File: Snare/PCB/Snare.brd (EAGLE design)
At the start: 100 x 50 mm, 93 parts, among them IC1 LM741P, IC10 LM741P, IC6 LM741P, IC7 LM741P, IC8 LM741P, IC9 LM741P, Q3 2N2222A, Q4 2N2222A, T1 2N3904, T5 2N3904, T6 2N3904

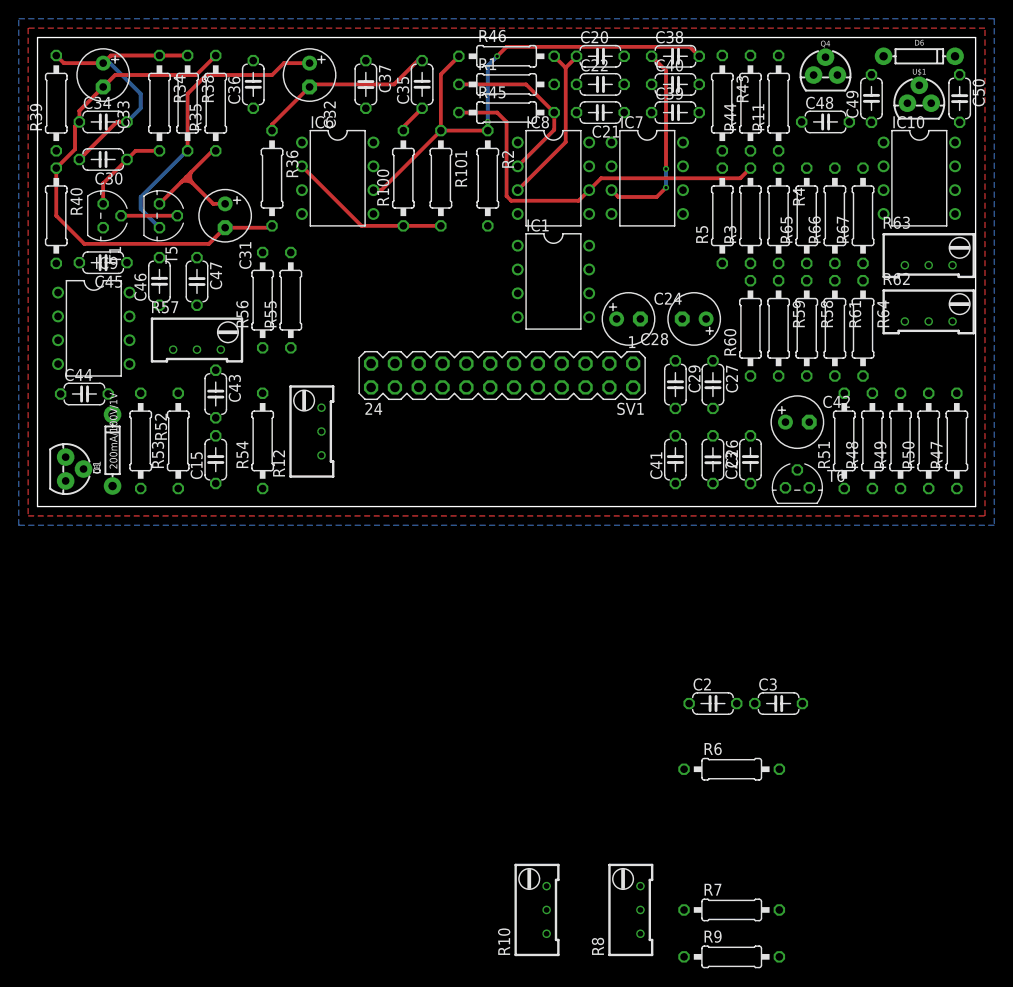
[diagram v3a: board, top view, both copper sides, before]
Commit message: Finished PCB
Finished the snare PCB
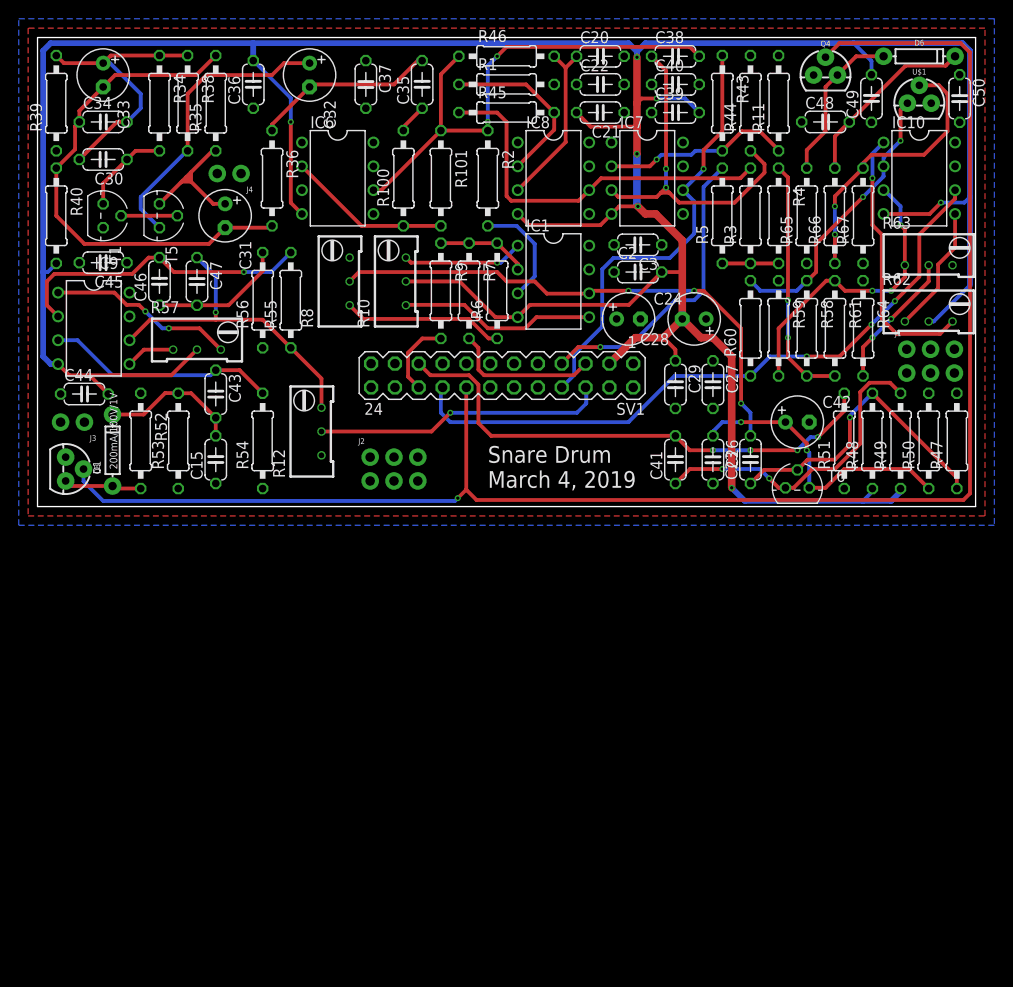
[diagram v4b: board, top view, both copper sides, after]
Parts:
- added J1, J2: (no value), SparkFun-Connectors:2X3-NS
- added J3, J4: (no value), SparkFun-Connectors:1X02_NO_SILK
- moved R9 77.5 mm to (43.0, 23.0), turned to 270 degrees
- moved R8 73.8 mm to (32.0, 24.0)
- moved R7 71.7 mm to (46.0, 23.0), turned to 270 degrees
- moved R10 68.7 mm to (38.0, 24.0)
- moved R6 56.8 mm to (49.0, 23.0), turned to 90 degrees
- moved C3 51.1 mm to (64.0, 27.9), turned to 180 degrees
- moved C2 46.7 mm to (64.0, 25.0)
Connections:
- removed net N$44: C46.1, C47.2
- new net N$8: C46.1, C47.2, R56.2
- net DRUM_OUTPUT: no longer R56.2
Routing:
- net -12V: track 0.00 -> 368.8 mm, vias 0 -> 7
- net TRIGGER: track 0.00 -> 172.3 mm, vias 0 -> 1
- net SW1: track 0.00 -> 71.4 mm, vias 0 -> 3
- net CC_INPUT: track 0.00 -> 56.8 mm, vias 0 -> 3
- net OUTPUT: track 0.00 -> 55.2 mm, vias 0 -> 4
- net POT2A: track 0.00 -> 47.0 mm, vias 0 -> 1
- net DRUM_OUTPUT: track 0.00 -> 34.5 mm, vias 0 -> 1
- net N$38: track 0.00 -> 33.8 mm, vias 0 -> 2
- net N$43: track 0.00 -> 32.8 mm, vias 0 -> 1
- net N$37: track 0.00 -> 32.7 mm, vias 0 -> 1
- net POT2B: track 0.00 -> 32.2 mm, vias 0 -> 1
- net N$48: track 0.00 -> 32.0 mm, vias 0 -> 3
- net POT1A: track 0.00 -> 31.2 mm, vias 0 -> 1
- net N$39: track 0.00 -> 31.1 mm, vias 0 -> 2
- net N$49: track 0.00 -> 30.4 mm, vias 0 -> 2
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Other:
- board text added: "Snare Drum March 4, 2019"

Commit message: Finished Silkscreen
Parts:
- removed C38: 1nF, resistor:C050-024X044
- removed C41: 2.2u, resistor:C050-024X044
- removed C42: 10uF, rcl:E2,5-6
- removed C43, C44, C45, C49, C50: 0.1uF, resistor:C050-024X044
- removed C47: 33nF, resistor:C050-024X044
- removed D6: 200mA/100V/1V, SparkFun-DiscreteSemi:DIODE-1N4148
- removed R100, R51: 47k, resistor:0207/10
- removed R101: 100k, resistor:0207/10
- removed R34: 680k, resistor:0207/10
- removed R39, R40: 2k, resistor:0207/10
- removed R46: 15k, resistor:0207/10
- removed R49: 10k, resistor:0207/10
- removed R50: 220, resistor:0207/10
- added C10, C6, C9: 0.1uF, resistor:C050-024X044
- added C13, C14, C16: 10uF, rcl:E2,5-6
- added C17, C18: 1u, resistor:C050-024X044
- added C4: 1nF, resistor:C050-024X044
- added D2: 200mA/100V/1V, SparkFun-DiscreteSemi:DIODE-1N4148
- added R13: 1k, resistor:0207/10
- added R14, R16: 100k, resistor:0207/10
- added R15, R17, R18: 10k, resistor:0207/10
- added TRIM3, TRIM4, TRIM6: 10k, rcl:RTRIM64W
- C15: value 0.33uF -> 10uF; device resistor:C050-024X044 -> rcl:E2,5-6
- C2: value 0.1uF -> 1nF
- C20: value 1nF -> 0.33uF
- C23: value 2.2u -> 0.1uF
- C24, C28: value 10uF -> 0.1uF; device rcl:E2,5-6 -> resistor:C050-024X044
- C26, C29: value 1u -> 0.1uF
- C27: value 1u -> 33nF
- C3: value 0.1uF -> 10uF; device resistor:C050-024X044 -> rcl:E2,5-6
- C30: value 0.1uF -> 2.2u
- C31: value 10uF -> 1u; device rcl:E2,5-6 -> resistor:C050-024X044
- C32: value 10uF -> 2.2u; device rcl:E2,5-6 -> resistor:C050-024X044
- R1: value 2k -> 15k
- R10: device rcl:RTRIM64W -> resistor:0207/10
- R11: value 4.7k -> 2k
- R12: value 10k -> 4.7k; device rcl:RTRIM64W -> resistor:0207/10
- R2: value 100k -> 47k
- R3, R4: value 10k -> 2k
- R35: value 1k -> 10k
- R36: value 100k -> 10k
- R38: value 4.7k -> 1k
- R43: value 2k -> 220
- R44: value 15k -> 10k
- R45: value 10k -> 47k
- R5: value 10k -> 15k
- R6: value 1k -> 2k
- R7: value 10k -> 4.7k
- R8: value 10k -> 680k; device rcl:RTRIM64W -> resistor:0207/10
- R9: value 10k -> 100k
- moved D1 95.7 mm to (94.0, 48.0), turned to 0 degrees
- moved Q3 91.2 mm to (84.0, 46.0), turned to 0 degrees
- moved Q4 91.2 mm to (3.00, 4.00), turned to 270 degrees
- moved C33 82.7 mm to (81.0, 9.00), turned to 0 degrees
- moved R4 77.0 mm to (2.00, 31.0)
- moved C30 76.1 mm to (76.0, 5.00), turned to 90 degrees
- moved R3 75.0 mm to (2.00, 43.0)
- moved C23 72.1 mm to (7.00, 26.0), turned to 180 degrees
- moved C26 67.4 mm to (5.00, 12.0), turned to 0 degrees
- moved C3 59.8 mm to (7.00, 46.0), turned to 270 degrees
- moved C20 59.4 mm to (19.0, 5.00), turned to 90 degrees
- moved C31 58.1 mm to (72.0, 5.00)
- moved C32 56.6 mm to (68.0, 5.00), turned to 90 degrees
- moved C27 56.1 mm to (17.0, 24.0)
- moved C22 52.6 mm to (19.0, 12.0), turned to 270 degrees
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- renumbered C34 to C5, C35 to C1, C36 to C8, C37 to C7, C39 to C12, C40 to C11, C46 to C25, C48 to C19, IC10 to IC4, IC7 to IC3, IC8 to IC2, IC9 to IC5, R47 to R41, R48 to R42, R52 to R20, R53 to R27, R54 to R29, R55 to R31, R56 to R32, R57 to TRIM5, R58 to R21, R59 to R28, R60 to R30, R61 to R22, R62 to TRIM2, R63 to TRIM1, R64 to R23, R65 to R19, R66 to R25, R67 to R26, T1 to Q1, T5 to Q2, T6 to Q6, U$1 to Q5
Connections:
- net +12V: now also C15.+, C17.2, C21.2, C23.1, C28.2, C9.2, R3.1, R43.2; no longer C22.2, C24.+, C27.2, C3.2, C45.1, C50.2, R39.1, R50.2
- net -12V: now also C10.2, C16.-, C18.1, C24.2, C26.2, C29.2, R4.2, R44.1, TRIM4.2; no longer C2.2, C21.2, C28.-, C29.1, C44.2, C49.2, R10.2, R40.2, R49.1
- net AGND: now also C10.1, C15.-, C16.+, C17.1, C18.2, C20.1, C23.2, C24.1, C26.1, C28.1, C29.1, C31.2, C33.-, C4.2, C9.1, R14.2, R45.1, R5.2, R6.2, R7.2, TRIM6.1; no longer C15.1, C2.1, C20.2, C22.1, C24.-, C26.2, C27.1, C28.+, C29.2, C3.1, C42.-, C44.1, C45.2, C49.1, C50.1, R1.2, R11.2, R12.1, R2.2, R44.2, R51.1
- net CC_INPUT: now also C30.2, IC6.6, TRIM3.2; no longer C23.2, IC1.6, R8.2
- net DRUM_OUTPUT: now also C27.1, TRIM6.3; no longer C47.1, R12.3
- net LOW_FREQ_WN: now also R10.1, R15.2; no longer R3.2, R45.1
- net N$1: now also R15.1, R17.1, R18.2; no longer R3.1, R4.2, R5.1
- net N$2: now also IC6.2, R35.1, R36.1, R38.2; no longer IC1.2, R6.2, R7.1, R9.1
- net N$20: now also C6.1, R8.2; no longer C30.1, R34.2
- net N$21: now also C14.-, C3.-, R13.2, R16.2, R4.1; no longer C31.-, C33.-, R35.2, R36.2, R40.1
- net N$23: now also IC1.2, R2.1, R9.2; no longer IC6.2, R100.1, R101.2
- net N$27: now also R11.2, R7.1; no longer R11.1, R43.2
- net N$28: now also R2.2; no longer R100.2
- net N$3: now also R38.1, TRIM3.1; no longer R6.1, R8.1
- net N$30: now also C13.+, R12.2; no longer C32.+, R38.2
- net N$32: now also C2.1, R5.1; no longer C38.1, R44.1
- net N$33: now also R10.2, R6.1; no longer R1.1, R45.2
- net N$34: now also C4.1, R1.2; no longer C20.1, R46.2
- net N$36: now also C20.2, C22.2, D2.C; no longer C15.2, C43.2, D1.C
- net N$37: now also C30.1; no longer C23.1
- net N$38: now also C32.1, R44.2; no longer C41.1, R49.2
- net N$39: now also C31.1, C33.+, R43.1; no longer C26.1, C42.+, R50.1
- net N$4: now also IC6.5, TRIM4.1; no longer IC1.5, R10.1
- net N$40: now also D2.A, Q4.3; no longer D1.A, Q3.3
- net N$41: now also C22.1; no longer C43.1
- net N$5: now also C14.+, R13.1; no longer C31.+, R35.1
- net N$51: now also D1.C; no longer D6.C
- net N$53: now also D1.A, Q3.3; no longer D6.A, Q4.3
- net N$6: now also C3.+, C6.2, R12.1, R3.2, R8.1; no longer C30.2, C33.+, R34.1, R38.1, R39.2
- net N$7: now also IC6.1, TRIM4.3; no longer IC1.1, R10.3
- net N$8: now also C27.2; no longer C47.2
- net OUTPUT: now also C32.2, R45.2; no longer C41.2, R51.2
- net POT1A: now also TRIM6.2; no longer R12.2
- net POT1B: now also R35.2; no longer R7.2
- net POT2A: now also R11.1; no longer R43.1
- net POT2B: now also R17.2; no longer R5.2
- net SW2: now also R36.2; no longer R9.2
- net VCA_INPUT: now also R18.1; no longer R4.1
- net WHITE_NOISE: now also C13.-, R16.1; no longer C32.-, R36.1
- net WHITE_NOISE_AMP: now also C2.2, IC1.6, R1.1, R14.1, R9.1; no longer C38.2, IC6.6, R101.1, R2.1, R46.1
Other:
- board text removed: "0V"
- board text removed: "OUT"
- board text removed: "TRIG"

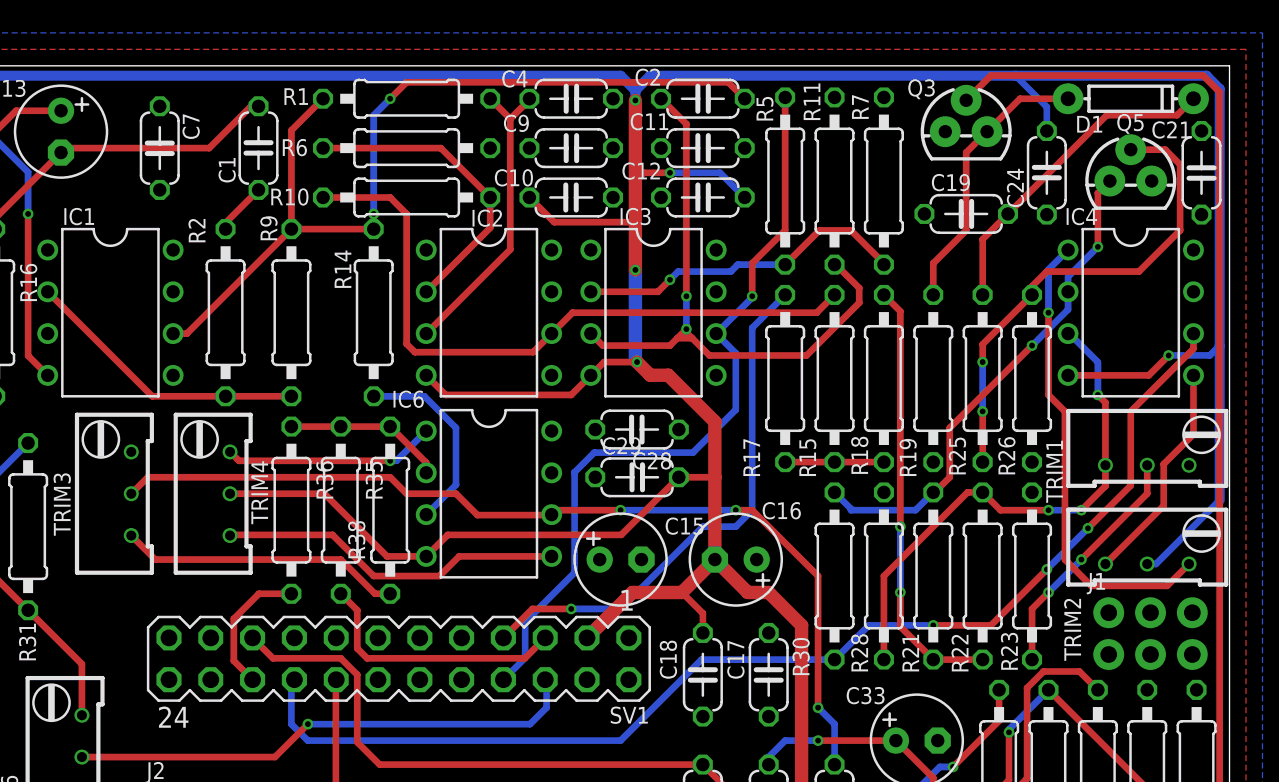
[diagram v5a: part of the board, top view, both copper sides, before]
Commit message: Added a few missing components
Added a few missing components. 3 coupling capacitors were missing
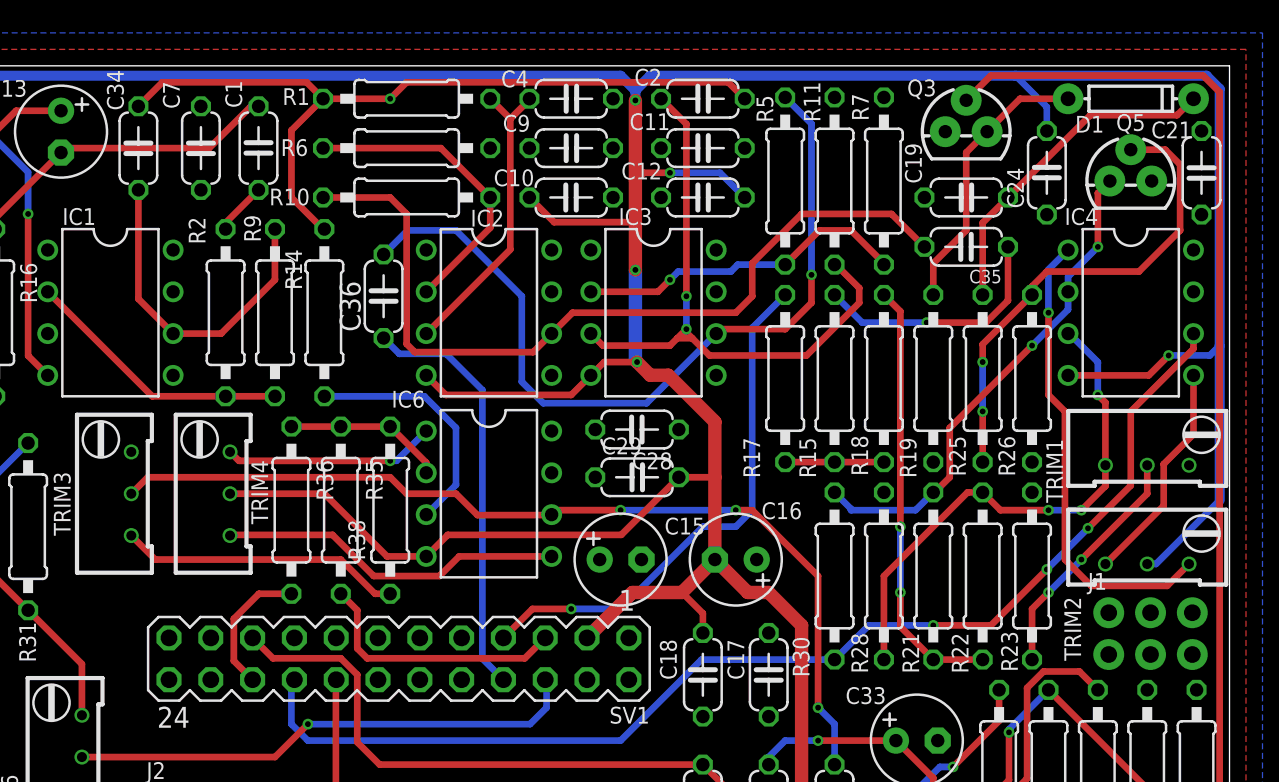
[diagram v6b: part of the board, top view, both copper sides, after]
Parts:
- added C34, C35, C36: 0.1uF, resistor:C050-024X044
- moved R14 3.00 mm to (45.0, 35.0)
- moved C7 2.50 mm to (37.5, 45.0)
- moved C19 1.00 mm to (84.0, 42.0)
- moved R9 1.00 mm to (42.0, 35.0)
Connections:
- new net HIGH_FREQ_WN: C36.2, IC3.6, R11.1
- new net N$10: C35.1, R15.2
- new net N$9: C34.2, IC1.6, R9.1
- net LOW_FREQ_WN: now also C35.2; no longer R15.2
- net POT2A: now also C36.1; no longer IC3.6, R11.1
- net WHITE_NOISE_AMP: now also C34.1; no longer IC1.6, R9.1
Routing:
- net HIGH_FREQ_WN: track 0.00 -> 49.7 mm, vias 0 -> 1
- net POT2A: track 47.0 -> 25.4 mm, vias 1 -> 0
- net N$9: track 0.00 -> 20.2 mm
- net N$10: track 0.00 -> 15.1 mm, vias 0 -> 1
- net LOW_FREQ_WN: track 41.0 -> 50.5 mm
- net WHITE_NOISE_AMP: track 54.2 -> 48.3 mm, vias 2 -> 1
- net AGND: track 11.8 -> 14.8 mm
- net N$23: track 17.4 -> 16.4 mm
- net N$51: track 19.7 -> 20.3 mm
